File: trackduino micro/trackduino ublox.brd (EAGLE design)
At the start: 52.6 x 22.3 mm, 31 parts, among them IC1 74AHC1G125DBV, IC2 74AHC1G125DBV, IC3 74AHC1G125DBV, U1 ATMEGA168

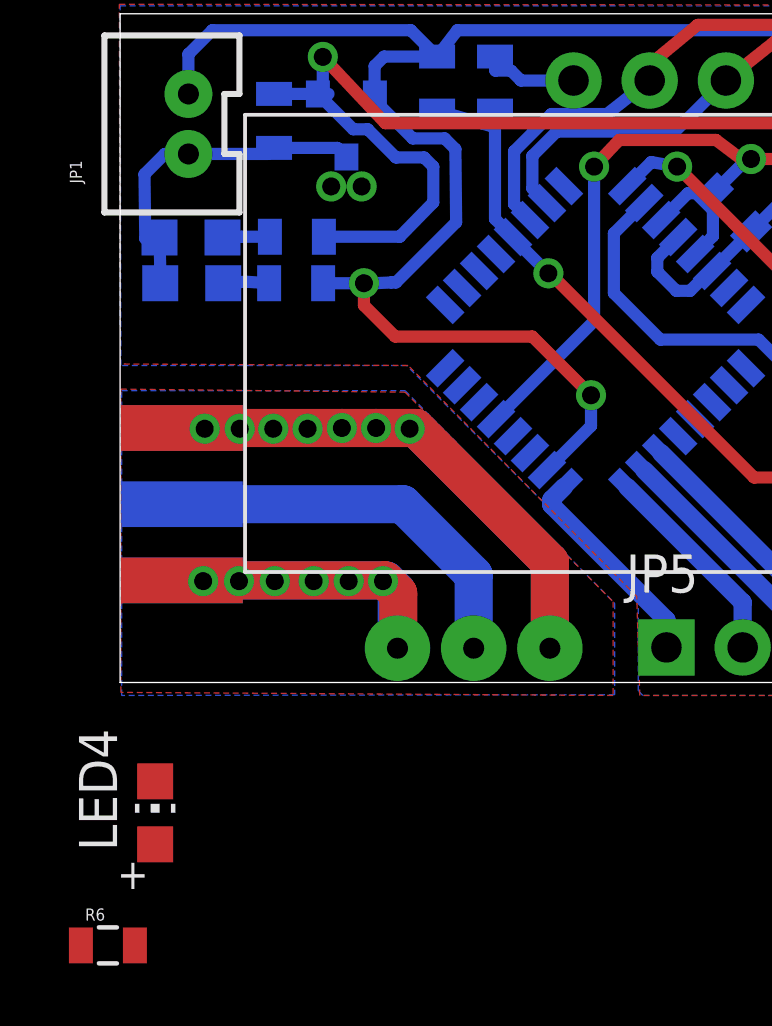
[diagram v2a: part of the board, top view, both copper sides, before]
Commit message: added status LED
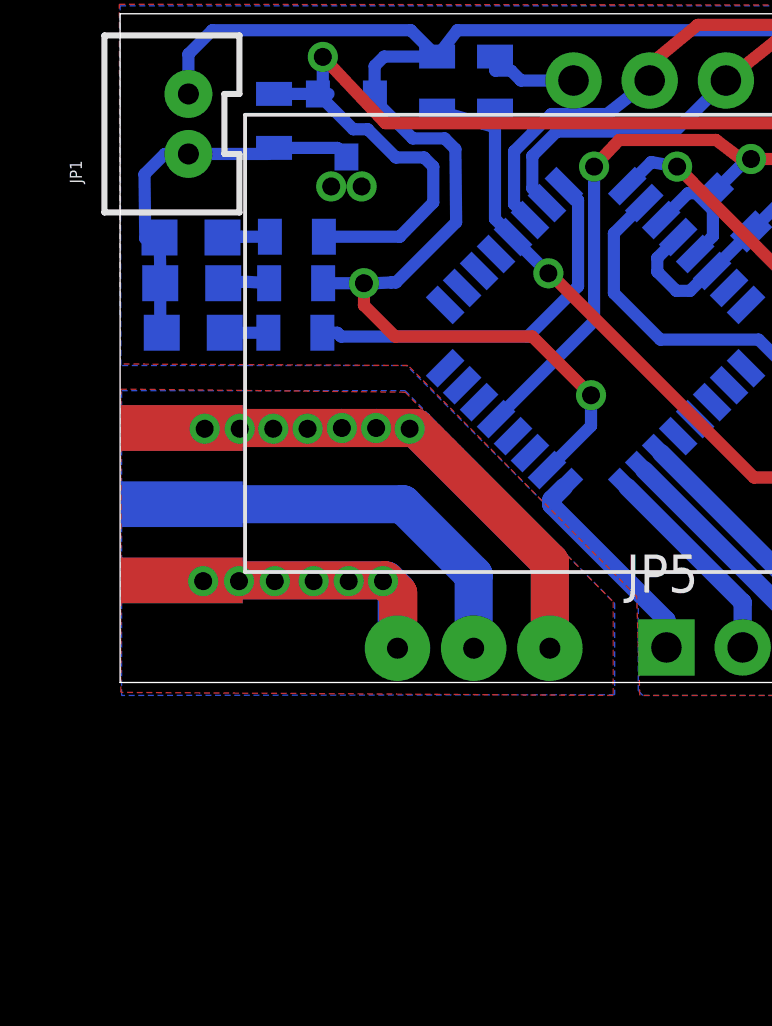
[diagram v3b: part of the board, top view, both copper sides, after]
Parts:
- moved R6 21.4 mm to (52.5, 69.1), flipped to the bottom, turned to 180 degrees
- moved LED4 16.1 mm to (49.1, 69.1), flipped to the bottom, turned to 270 degrees
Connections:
- new net LED: R6.2, U1.32
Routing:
- net LED: track 0.00 -> 12.8 mm
- net GND: track 171.6 -> 173.3 mm
- net N$14: track 0.00 -> 1.45 mm
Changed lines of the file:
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@@
 <attribute name="PROD_ID" value="SWCH-08247" x="95.631" y="60.1218" size="1.778" layer="27" display="off"/>
 </element>
-<element name="LED4" library="adafruit" package="CHIP-LED0805" value="" x="47.8282" y="53.1114"/>
-<element name="R6" library="SparkFun-Resistors" package="0805" value="" x="46.2534" y="48.6918"/>
+<element name="LED4" library="adafruit" package="CHIP-LED0805" value="" x="49.0982" y="69.1134" rot="MR270"/>
+<element name="R6" library="SparkFun-Resistors" package="0805" value="" x="52.5018" y="69.1134" rot="MR180"/>
 </elements>
 <signals>
@@
 <wire x1="65.827571875" y1="71.73888125" x2="66.41960625" y2="72.330915625" width="0.4064" layer="16"/>
 <wire x1="66.41960625" y1="72.330915625" x2="66.41960625" y2="73.76299375" width="0.4064" layer="16"/>
+<wire x1="48.0482" y1="69.1134" x2="47.9974" y2="69.1642" width="0.4064" layer="16"/>
+<wire x1="47.9974" y1="69.1642" x2="47.9974" y2="70.7644" width="0.4064" layer="16"/>
 <wire x1="96.6978" y1="64.1604" x2="98.425" y2="58.2168" width="0" layer="19" extent="1-1"/>
 <wire x1="96.9772" y1="64.262" x2="96.9772" y2="64.262" width="0" layer="19" extent="1-16"/>
@@
 <wire x1="55.9562" y1="58.6232" x2="60.9854" y2="58.5978" width="0" layer="19" extent="1-1"/>
 <wire x1="48.7172" y1="60.8584" x2="48.7172" y2="60.8584" width="0" layer="19" extent="1-16"/>
-<wire x1="47.8282" y1="54.1614" x2="48.7172" y2="60.8584" width="0" layer="19" extent="1-1"/>
 </signal>
 <signal name="VCC">
@@
 <contactref element="LED4" pad="A"/>
 <contactref element="R6" pad="1"/>
-<wire x1="45.3534" y1="48.6918" x2="47.8282" y2="52.0614" width="0" layer="19" extent="1-1"/>
+<wire x1="50.1482" y1="69.1134" x2="51.6018" y2="69.1134" width="0.4064" layer="16"/>
 </signal>
 <signal name="N$26">
@@
 <via x="54.7116" y="73.9902" extent="1-16" drill="0.6" shape="square"/>
 </signal>
+<signal name="LED">
+<contactref element="U1" pad="32"/>
+<contactref element="R6" pad="2"/>
+<wire x1="61.453975" y1="74.001625" x2="61.9252" y2="73.5304" width="0.4064" layer="16"/>
+<wire x1="61.9252" y1="73.5304" x2="61.9252" y2="70.6628" width="0.4064" layer="16"/>
+<wire x1="61.9252" y1="70.6628" x2="60.2488" y2="68.9864" width="0.4064" layer="16"/>
+<wire x1="60.2488" y1="68.9864" x2="54.0258" y2="68.9864" width="0.4064" layer="16"/>
+<wire x1="54.0258" y1="68.9864" x2="53.8988" y2="69.1134" width="0.4064" layer="16"/>
+<wire x1="53.8988" y1="69.1134" x2="53.4018" y2="69.1134" width="0.4064" layer="16"/>
+</signal>
 </signals>
